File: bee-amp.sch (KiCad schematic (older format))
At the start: 4 parts, among them J1 Conn_01x02_Male, J2 Conn_01x02_Male, J3 Conn_01x02_Male, J4 Conn_01x02_Male

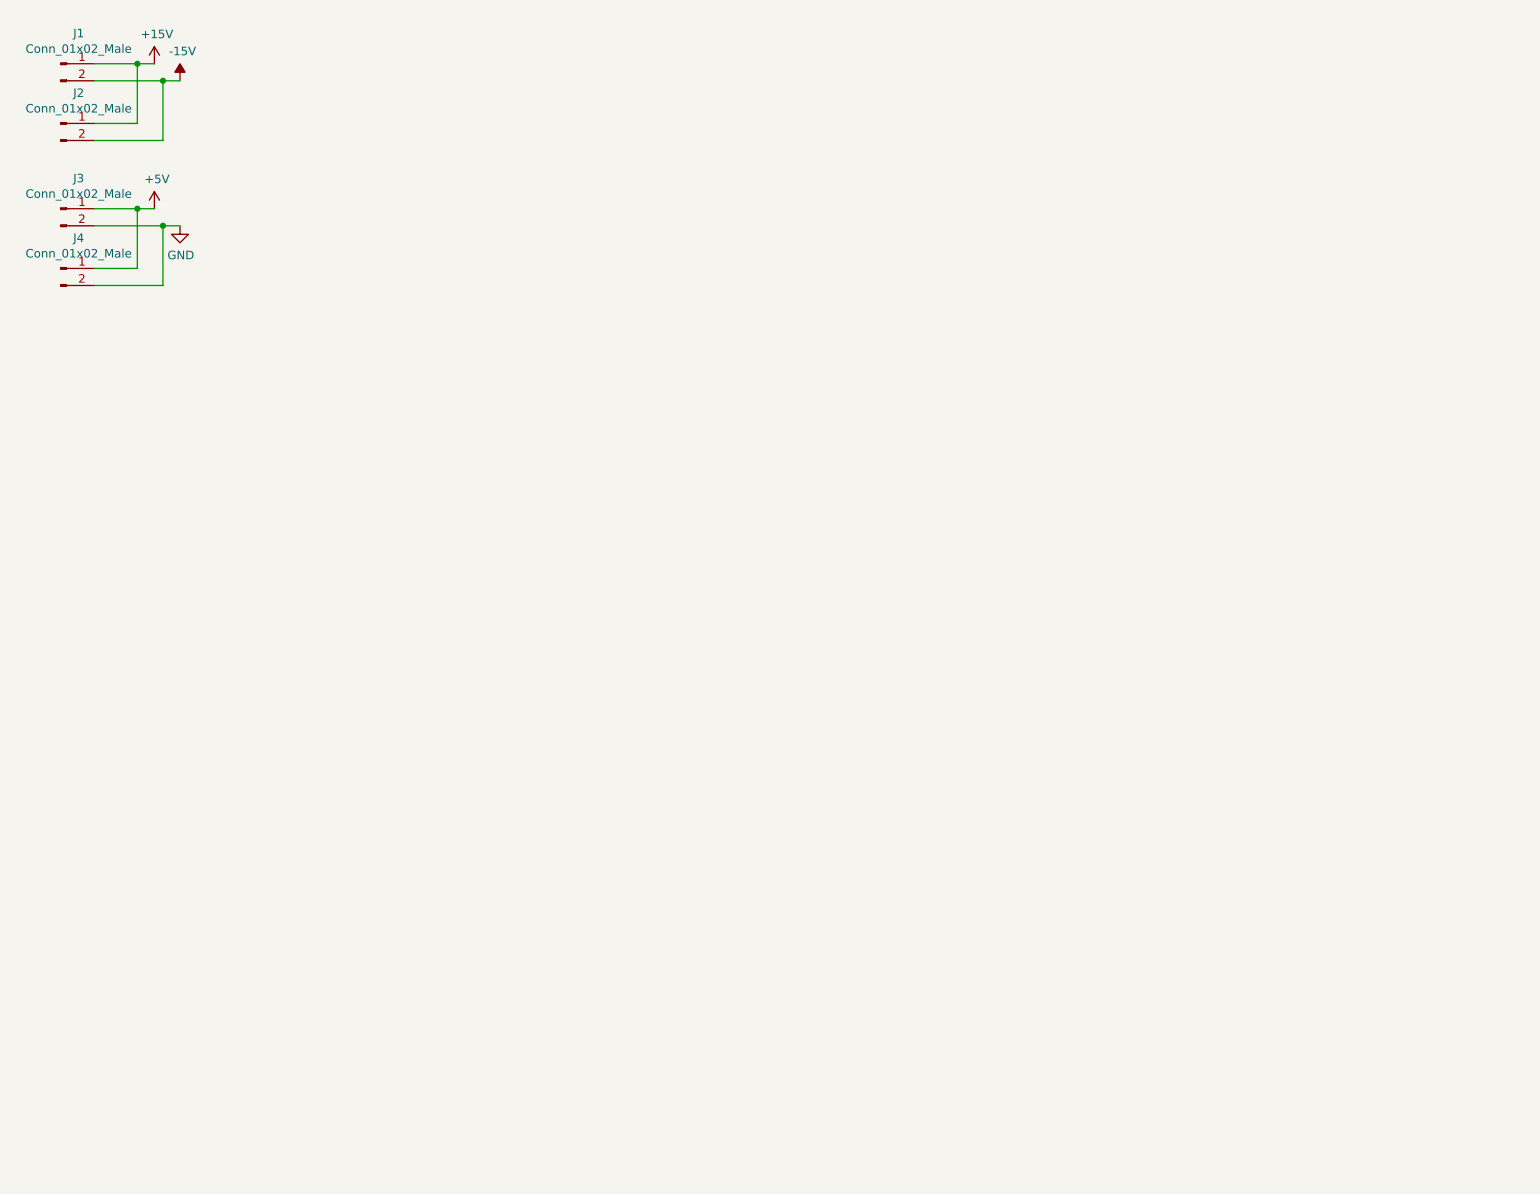
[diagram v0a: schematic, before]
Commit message: schematic and basic layout
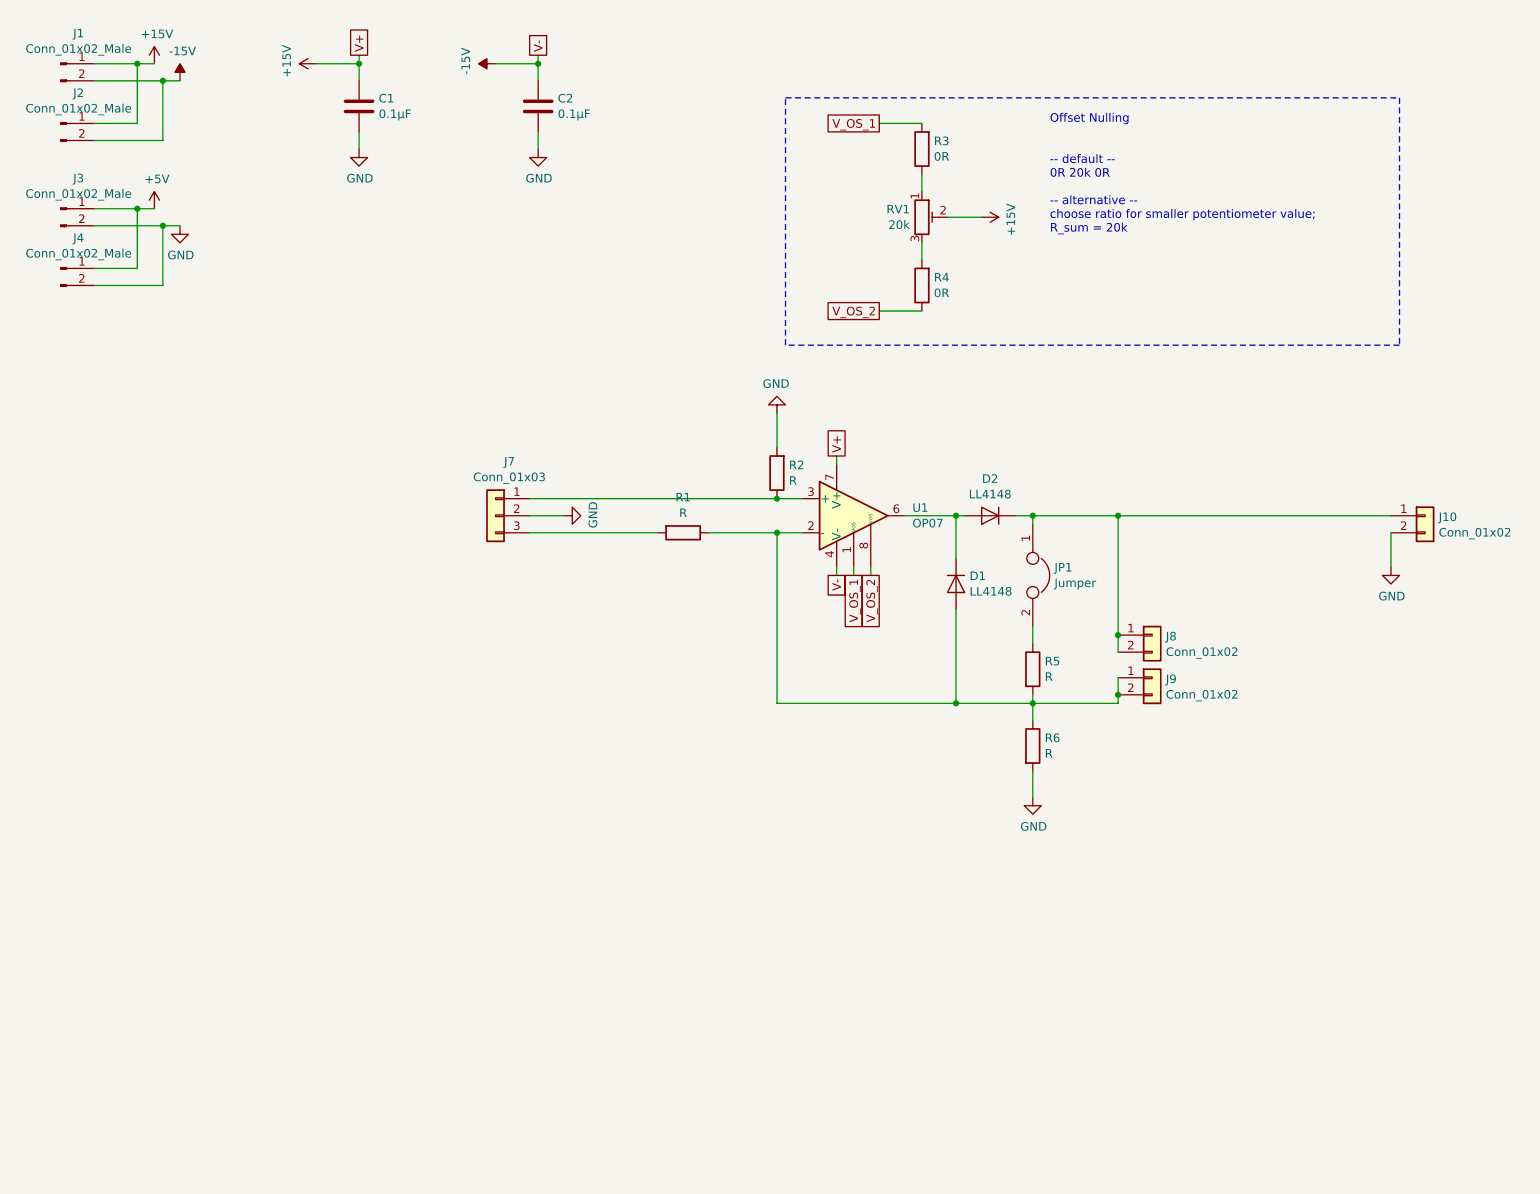
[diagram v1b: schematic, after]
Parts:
- added C1, C2: 0.1µF, Capacitor_SMD:C_0805_2012Metric_Pad1.15x1.40mm_HandSolder, symbol Device:C
- added D1, D2: LL4148, Diode_SMD:D_MiniMELF, symbol Diode:LL4148
- added J10: Conn_01x02, Connector_PinHeader_2.54mm:PinHeader_1x02_P2.54mm_Vertical, symbol Connector_Generic:Conn_01x02
- added J7: Conn_01x03, Connector_PinHeader_2.54mm:PinHeader_1x03_P2.54mm_Vertical, symbol Connector_Generic:Conn_01x03
- added J8, J9: Conn_01x02, Connector_PinSocket_2.54mm:PinSocket_1x02_P2.54mm_Vertical, symbol Connector_Generic:Conn_01x02
- added JP1: Jumper, Connector_PinHeader_2.54mm:PinHeader_1x02_P2.54mm_Vertical, symbol Device:Jumper
- added R1, R2, R5, R6: R, Resistor_SMD:R_0805_2012Metric_Pad1.15x1.40mm_HandSolder, symbol Device:R
- added R3, R4: 0R, Resistor_SMD:R_0805_2012Metric_Pad1.15x1.40mm_HandSolder, symbol Device:R
- added RV1: 20k, Potentiometer_SMD:Potentiometer_Bourns_3314J_Vertical, symbol Device:R_POT_TRIM
- added U1: OP07, Package_SO:SO-8_5.3x6.2mm_P1.27mm, symbol Amplifier_Operational:OP07
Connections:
- net +15V: now also C1.1, RV1.2, U1.7 (V+)
- net -15V: now also C2.1, U1.4 (V-)
- net GND: now also C1.2, C2.2, J10.2 (Pin_2), J7.2 (Pin_2), R2.2, R6.2
- new net: D1.2 (A), J9.1 (Pin_1), J9.2 (Pin_2), R1.1, R5.2, R6.1, U1.2 (-)
- new net: J7.1 (Pin_1), R2.1, U1.3 (+)
- new net: D1.1 (K), D2.2 (A), U1.6
- new net: J7.3 (Pin_3), R1.2
- new net: D2.1 (K), J10.1 (Pin_1), J8.1 (Pin_1), J8.2 (Pin_2), JP1.1
- new net: JP1.2, R5.1
- new net: R3.1, RV1.1
- new net: R4.2, RV1.3
- new net V_OS_1: R3.2, U1.1 (VOS)
- new net V_OS_2: R4.1, U1.8 (VOS)
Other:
- note added: "Offset Nulling\n\n\n-- default --\n0R 20k 0R\n\n-- alternative --\nchoose ratio for smaller potentiometer value;\nR_sum = 20k"

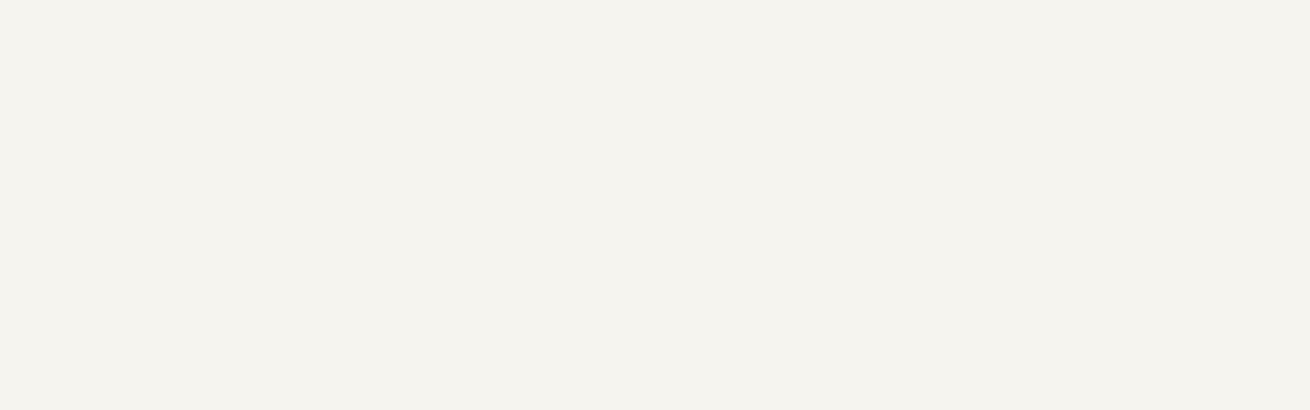
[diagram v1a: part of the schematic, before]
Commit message: Update lables and mounting holes.
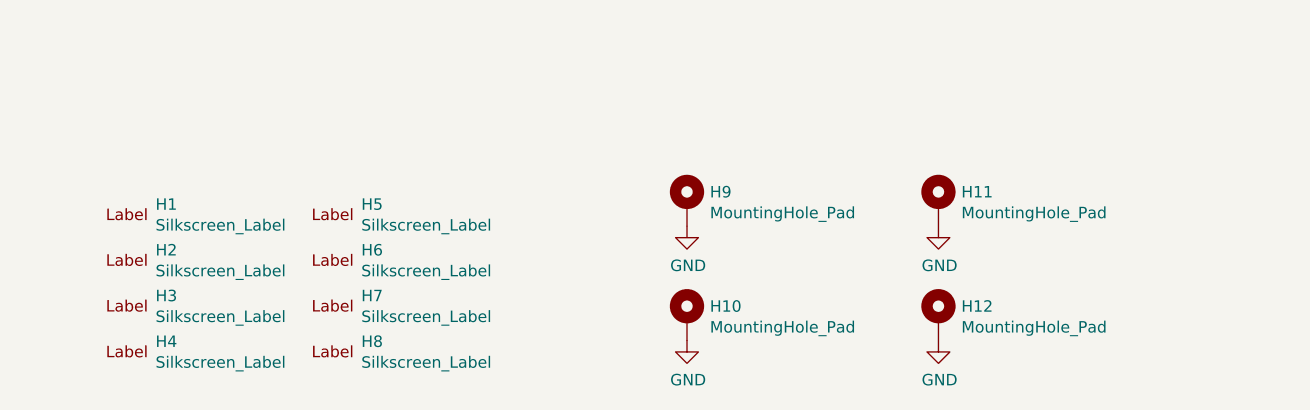
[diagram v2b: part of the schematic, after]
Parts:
- added H1, H2: Silkscreen_Label, Symbol-emt:Text_U_B+_Silkscreen, symbol Mechanical-emt:Silkscreen_Label
- added H10, H11, H12, H9: MountingHole_Pad, MountingHole:MountingHole_3.2mm_M3_ISO7380_Pad, symbol Mechanical:MountingHole_Pad
- added H3, H4: Silkscreen_Label, Symbol-emt:Text_U_B-_Silkscreen, symbol Mechanical-emt:Silkscreen_Label
- added H5, H6: Silkscreen_Label, Symbol-emt:Text_U_B2_Silkscreen, symbol Mechanical-emt:Silkscreen_Label
- added H7, H8: Silkscreen_Label, Symbol-emt:Symbol_GND_Silkscreen, symbol Mechanical-emt:Silkscreen_Label
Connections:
- net GND: now also H10.1, H11.1, H12.1, H9.1
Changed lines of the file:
@@
 Wire Wire Line
 	5650 1300 5900 1300
+$Comp
+L Mechanical-emt:Silkscreen_Label H1
+U 1 1 5CCC8957
+P 1050 6600
+F 0 "H1" H 1175 6645 50  0000 L CNN
+F 1 "Silkscreen_Label" H 1175 6554 50  0000 L CNN
+F 2 "Symbol-emt:Text_U_B+_Silkscreen" H 1050 6600 50  0001 C CNN
+F 3 "~" H 1050 6600 50  0001 C CNN
+	1    1050 6600
+	1    0    0    -1
+$EndComp
+$Comp
+L Mechanical-emt:Silkscreen_Label H2
+U 1 1 5CCC93D9
+P 1050 6800
+F 0 "H2" H 1175 6845 50  0000 L CNN
+F 1 "Silkscreen_Label" H 1175 6754 50  0000 L CNN
+F 2 "Symbol-emt:Text_U_B+_Silkscreen" H 1050 6800 50  0001 C CNN
+F 3 "~" H 1050 6800 50  0001 C CNN
+	1    1050 6800
+	1    0    0    -1
+$EndComp
+$Comp
+L Mechanical-emt:Silkscreen_Label H3
+U 1 1 5CCCAC57
+P 1050 7000
+F 0 "H3" H 1175 7045 50  0000 L CNN
+F 1 "Silkscreen_Label" H 1175 6954 50  0000 L CNN
+F 2 "Symbol-emt:Text_U_B-_Silkscreen" H 1050 7000 50  0001 C CNN
+F 3 "~" H 1050 7000 50  0001 C CNN
+	1    1050 7000
+	1    0    0    -1
+$EndComp
+$Comp
+L Mechanical-emt:Silkscreen_Label H4
+U 1 1 5CCCAF9B
+P 1050 7200
+F 0 "H4" H 1175 7245 50  0000 L CNN
+F 1 "Silkscreen_Label" H 1175 7154 50  0000 L CNN
+F 2 "Symbol-emt:Text_U_B-_Silkscreen" H 1050 7200 50  0001 C CNN
+F 3 "~" H 1050 7200 50  0001 C CNN
+	1    1050 7200
+	1    0    0    -1
+$EndComp
+$Comp
+L Mechanical-emt:Silkscreen_Label H5
+U 1 1 5CCCB104
+P 1950 6600
+F 0 "H5" H 2075 6645 50  0000 L CNN
+F 1 "Silkscreen_Label" H 2075 6554 50  0000 L CNN
+F 2 "Symbol-emt:Text_U_B2_Silkscreen" H 1950 6600 50  0001 C CNN
+F 3 "~" H 1950 6600 50  0001 C CNN
+	1    1950 6600
+	1    0    0    -1
+$EndComp
+$Comp
+L Mechanical-emt:Silkscreen_Label H6
+U 1 1 5CCCB407
+P 1950 6800
+F 0 "H6" H 2075 6845 50  0000 L CNN
+F 1 "Silkscreen_Label" H 2075 6754 50  0000 L CNN
+F 2 "Symbol-emt:Text_U_B2_Silkscreen" H 1950 6800 50  0001 C CNN
+F 3 "~" H 1950 6800 50  0001 C CNN
+	1    1950 6800
+	1    0    0    -1
+$EndComp
+$Comp
+L Mechanical-emt:Silkscreen_Label H7
+U 1 1 5CCCB63D
+P 1950 7000
+F 0 "H7" H 2075 7045 50  0000 L CNN
+F 1 "Silkscreen_Label" H 2075 6954 50  0000 L CNN
+F 2 "Symbol-emt:Symbol_GND_Silkscreen" H 1950 7000 50  0001 C CNN
+F 3 "~" H 1950 7000 50  0001 C CNN
+	1    1950 7000
+	1    0    0    -1
+$EndComp
+$Comp
+L Mechanical-emt:Silkscreen_Label H8
+U 1 1 5CCCB8AF
+P 1950 7200
+F 0 "H8" H 2075 7245 50  0000 L CNN
+F 1 "Silkscreen_Label" H 2075 7154 50  0000 L CNN
+F 2 "Symbol-emt:Symbol_GND_Silkscreen" H 1950 7200 50  0001 C CNN
+F 3 "~" H 1950 7200 50  0001 C CNN
+	1    1950 7200
+	1    0    0    -1
+$EndComp
+$Comp
+L Mechanical:MountingHole_Pad H9
+U 1 1 5CCCE55F
+P 3500 6550
+F 0 "H9" H 3600 6599 50  0000 L CNN
+F 1 "MountingHole_Pad" H 3600 6508 50  0000 L CNN
+F 2 "MountingHole:MountingHole_3.2mm_M3_ISO7380_Pad" H 3500 6550 50  0001 C CNN
+F 3 "~" H 3500 6550 50  0001 C CNN
+	1    3500 6550
+	1    0    0    -1
+$EndComp
+$Comp
+L Mechanical:MountingHole_Pad H10
+U 1 1 5CCCEB49
+P 3500 7050
+F 0 "H10" H 3600 7099 50  0000 L CNN
+F 1 "MountingHole_Pad" H 3600 7008 50  0000 L CNN
+F 2 "MountingHole:MountingHole_3.2mm_M3_ISO7380_Pad" H 3500 7050 50  0001 C CNN
+F 3 "~" H 3500 7050 50  0001 C CNN
+	1    3500 7050
+	1    0    0    -1
+$EndComp
+$Comp
+L Mechanical:MountingHole_Pad H11
+U 1 1 5CCCF2D7
+P 4600 6550
+F 0 "H11" H 4700 6599 50  0000 L CNN
+F 1 "MountingHole_Pad" H 4700 6508 50  0000 L CNN
+F 2 "MountingHole:MountingHole_3.2mm_M3_ISO7380_Pad" H 4600 6550 50  0001 C CNN
+F 3 "~" H 4600 6550 50  0001 C CNN
+	1    4600 6550
+	1    0    0    -1
+$EndComp
+$Comp
+L Mechanical:MountingHole_Pad H12
+U 1 1 5CCCFC71
+P 4600 7050
+F 0 "H12" H 4700 7099 50  0000 L CNN
+F 1 "MountingHole_Pad" H 4700 7008 50  0000 L CNN
+F 2 "MountingHole:MountingHole_3.2mm_M3_ISO7380_Pad" H 4600 7050 50  0001 C CNN
+F 3 "~" H 4600 7050 50  0001 C CNN
+	1    4600 7050
+	1    0    0    -1
+$EndComp
+$Comp
+L power:GND #PWR0101
+U 1 1 5CCD0091
+P 3500 6650
+F 0 "#PWR0101" H 3500 6400 50  0001 C CNN
+F 1 "GND" H 3505 6477 50  0000 C CNN
+F 2 "" H 3500 6650 50  0001 C CNN
+F 3 "" H 3500 6650 50  0001 C CNN
+	1    3500 6650
+	1    0    0    -1
+$EndComp
+$Comp
+L power:GND #PWR0102
+U 1 1 5CCD07F8
+P 3500 7150
+F 0 "#PWR0102" H 3500 6900 50  0001 C CNN
+F 1 "GND" H 3505 6977 50  0000 C CNN
+F 2 "" H 3500 7150 50  0001 C CNN
+F 3 "" H 3500 7150 50  0001 C CNN
+	1    3500 7150
+	1    0    0    -1
+$EndComp
+$Comp
+L power:GND #PWR0103
+U 1 1 5CCD1530
+P 4600 6650
+F 0 "#PWR0103" H 4600 6400 50  0001 C CNN
+F 1 "GND" H 4605 6477 50  0000 C CNN
+F 2 "" H 4600 6650 50  0001 C CNN
+F 3 "" H 4600 6650 50  0001 C CNN
+	1    4600 6650
+	1    0    0    -1
+$EndComp
+$Comp
+L power:GND #PWR0104
+U 1 1 5CCD170F
+P 4600 7150
+F 0 "#PWR0104" H 4600 6900 50  0001 C CNN
+F 1 "GND" H 4605 6977 50  0000 C CNN
+F 2 "" H 4600 7150 50  0001 C CNN
+F 3 "" H 4600 7150 50  0001 C CNN
+	1    4600 7150
+	1    0    0    -1
+$EndComp
 $EndSCHEMATC

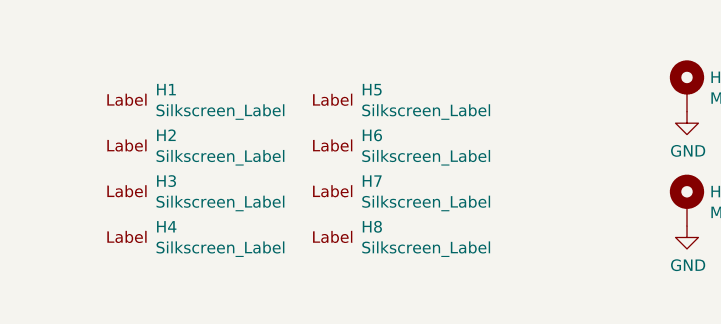
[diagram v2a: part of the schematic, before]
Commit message: Add text and logos.
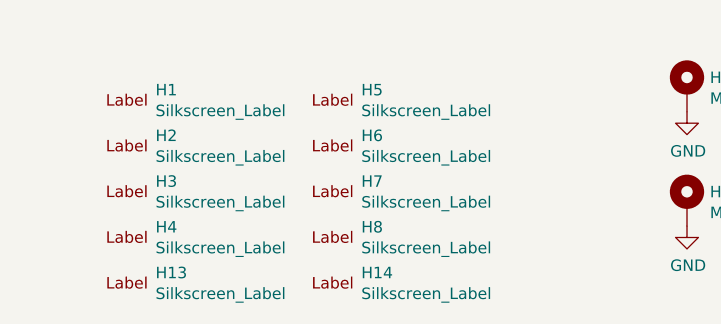
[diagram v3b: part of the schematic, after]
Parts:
- added H13: Silkscreen_Label, Symbol-emt:EMT-Logo_5.1x2.5mm_Silkscreen, symbol Mechanical-emt:Silkscreen_Label
- added H14: Silkscreen_Label, Symbol-emt:BEE-Logo_Silkscreen_small, symbol Mechanical-emt:Silkscreen_Label
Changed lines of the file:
@@
 EESchema Schematic File Version 4
 LIBS:bee-amp-cache
-EELAYER 29 0
+EELAYER 26 0
 EELAYER END
 $Descr A4 11693 8268
@@
 	1    0    0    -1
 $EndComp
+$Comp
+L Mechanical-emt:Silkscreen_Label H13
+U 1 1 5CCCB2BD
+P 1050 7400
+F 0 "H13" H 1175 7445 50  0000 L CNN
+F 1 "Silkscreen_Label" H 1175 7354 50  0000 L CNN
+F 2 "Symbol-emt:EMT-Logo_5.1x2.5mm_Silkscreen" H 1050 7400 50  0001 C CNN
+F 3 "~" H 1050 7400 50  0001 C CNN
+	1    1050 7400
+	1    0    0    -1
+$EndComp
+$Comp
+L Mechanical-emt:Silkscreen_Label H14
+U 1 1 5CCCB365
+P 1950 7400
+F 0 "H14" H 2075 7445 50  0000 L CNN
+F 1 "Silkscreen_Label" H 2075 7354 50  0000 L CNN
+F 2 "Symbol-emt:BEE-Logo_Silkscreen_small" H 1950 7400 50  0001 C CNN
+F 3 "~" H 1950 7400 50  0001 C CNN
+	1    1950 7400
+	1    0    0    -1
+$EndComp
